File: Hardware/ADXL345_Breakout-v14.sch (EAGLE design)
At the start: 10 parts, among them U2 ADXL345PATRICK

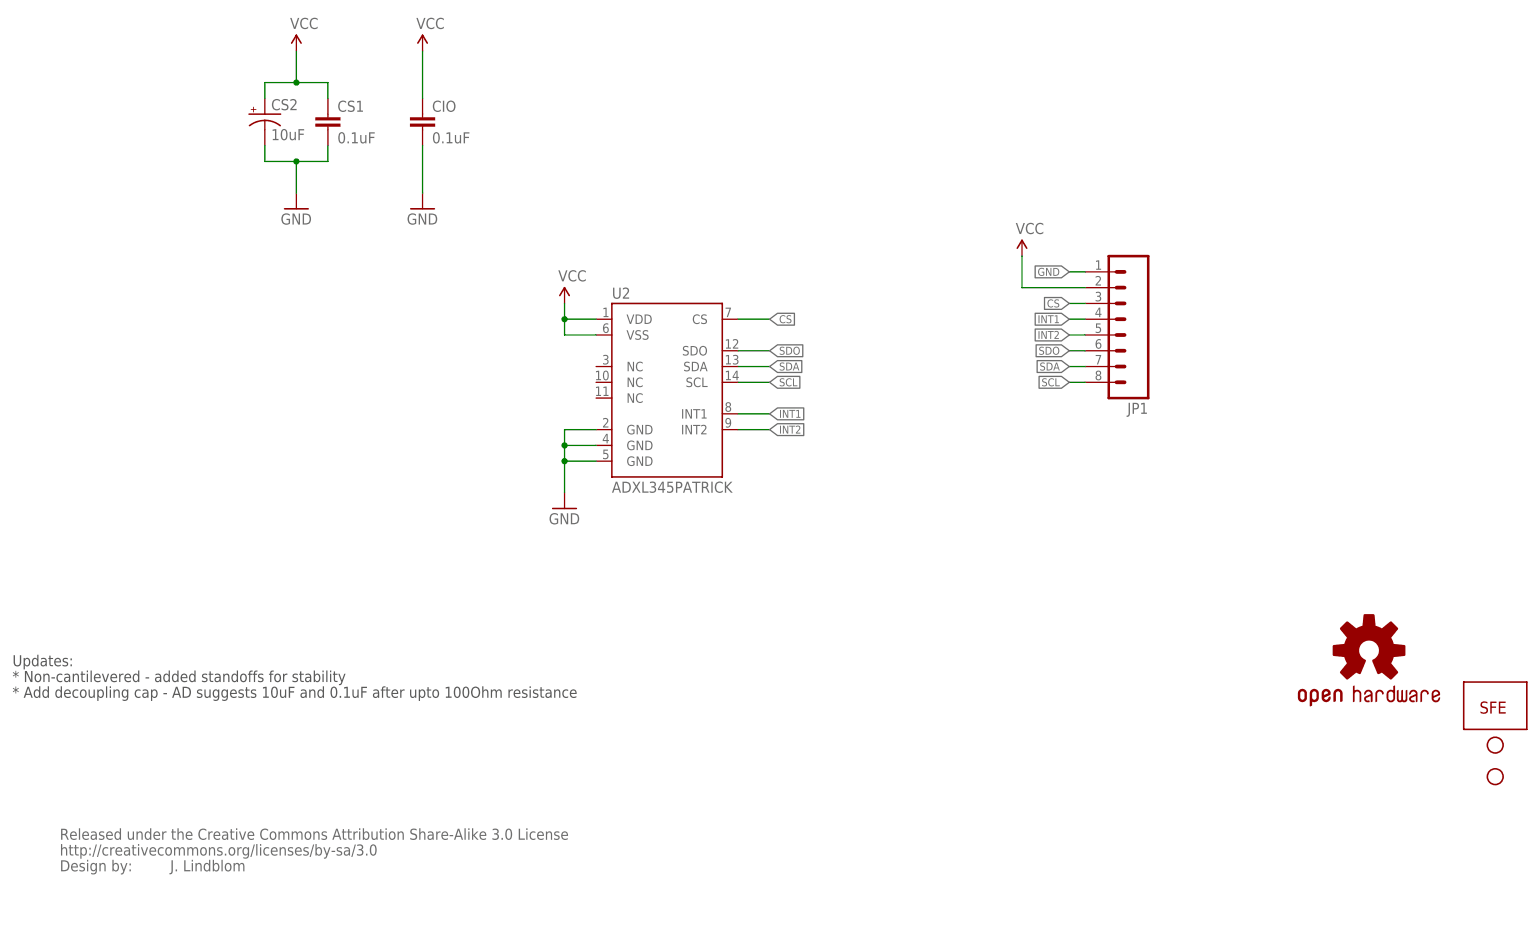
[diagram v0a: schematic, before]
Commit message: Schematic Change, CAP Names, Package Move
Updated to Frame Letter for the Schematic, Changed Caps names to C2, C1
and Moved the ADXL345 package to make more room for the 10uf Cap.
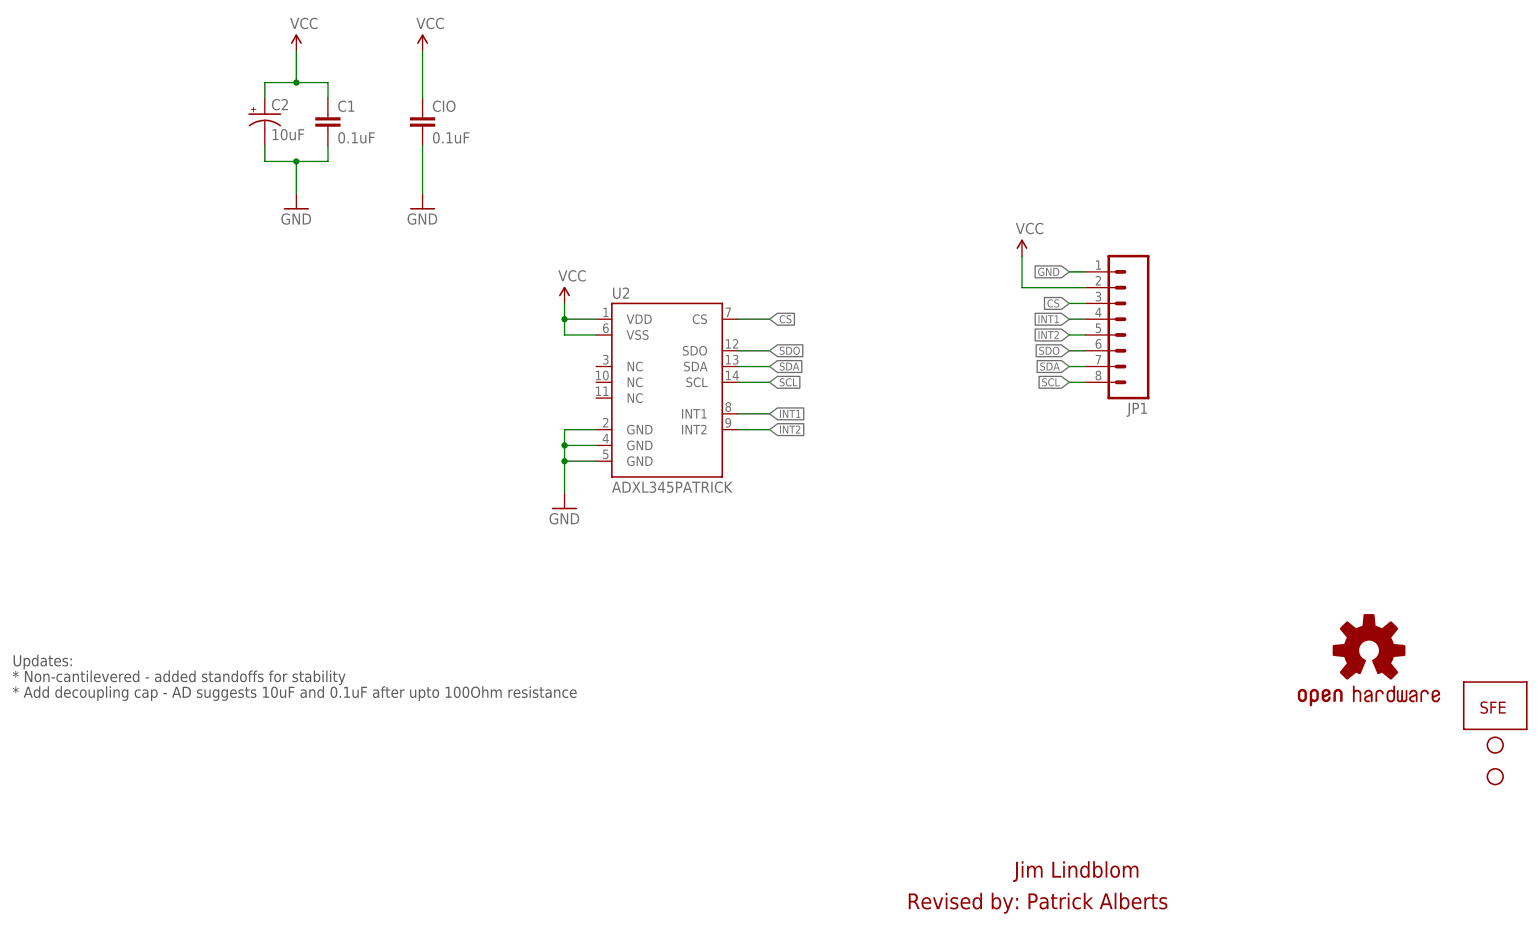
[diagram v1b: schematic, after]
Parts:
- removed U$1: CREATIVE_COMMONS, SparkFun:CREATIVE_COMMONS
- renumbered CS1 to C1, CS2 to C2
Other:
- note added: "Jim Lindblom"
- note added: "Revised by: Patrick Alberts"
- note removed: "J. Lindblom"

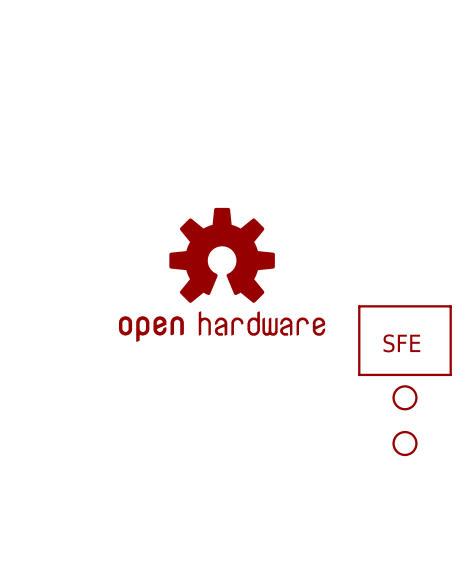
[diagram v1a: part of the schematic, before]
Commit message: Added fiducials
Forgot to put these on the protos, fiducials now added.
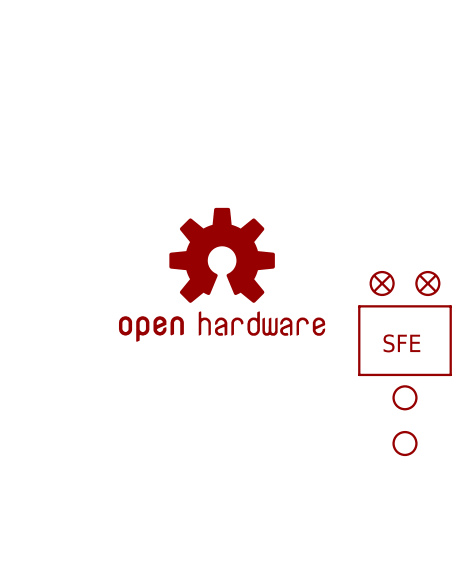
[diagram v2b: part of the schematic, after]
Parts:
- added JP4, JP5: FIDUCIAL1X2, SparkFun-Aesthetics:FIDUCIAL1X2
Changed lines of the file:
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@@
 <grid distance="0.1" unitdist="inch" unit="inch" style="lines" multiple="1" display="no" altdistance="0.01" altunitdist="inch" altunit="inch"/>
 <layers>
-<layer number="1" name="Top" color="4" fill="1" visible="yes" active="no"/>
-<layer number="2" name="Route2" color="1" fill="3" visible="yes" active="no"/>
-<layer number="3" name="Route3" color="4" fill="3" visible="yes" active="no"/>
-<layer number="4" name="Route4" color="1" fill="4" visible="yes" active="no"/>
-<layer number="5" name="Route5" color="4" fill="4" visible="yes" active="no"/>
-<layer number="6" name="Route6" color="1" fill="8" visible="yes" active="no"/>
-<layer number="7" name="Route7" color="4" fill="8" visible="yes" active="no"/>
-<layer number="8" name="Route8" color="1" fill="2" visible="yes" active="no"/>
-<layer number="9" name="Route9" color="4" fill="2" visible="yes" active="no"/>
-<layer number="10" name="Route10" color="1" fill="7" visible="yes" active="no"/>
-<layer number="11" name="Route11" color="4" fill="7" visible="yes" active="no"/>
-<layer number="12" name="Route12" color="1" fill="5" visible="yes" active="no"/>
-<layer number="13" name="Route13" color="4" fill="5" visible="yes" active="no"/>
-<layer number="14" name="Route14" color="1" fill="6" visible="yes" active="no"/>
-<layer number="15" name="Route15" color="4" fill="6" visible="yes" active="no"/>
-<layer number="16" name="Bottom" color="1" fill="1" visible="yes" active="no"/>
-<layer number="17" name="Pads" color="2" fill="1" visible="yes" active="no"/>
-<layer number="18" name="Vias" color="2" fill="1" visible="yes" active="no"/>
-<layer number="19" name="Unrouted" color="6" fill="1" visible="yes" active="no"/>
-<layer number="20" name="Dimension" color="15" fill="1" visible="yes" active="no"/>
-<layer number="21" name="tPlace" color="16" fill="1" visible="yes" active="no"/>
-<layer number="22" name="bPlace" color="14" fill="1" visible="yes" active="no"/>
-<layer number="23" name="tOrigins" color="15" fill="1" visible="yes" active="no"/>
-<layer number="24" name="bOrigins" color="15" fill="1" visible="yes" active="no"/>
-<layer number="25" name="tNames" color="7" fill="1" visible="yes" active="no"/>
-<layer number="26" name="bNames" color="7" fill="1" visible="yes" active="no"/>
-<layer number="27" name="tValues" color="7" fill="1" visible="yes" active="no"/>
-<layer number="28" name="bValues" color="7" fill="1" visible="yes" active="no"/>
+<layer number="1" name="Top" color="4" fill="1" visible="no" active="no"/>
+<layer number="2" name="Route2" color="1" fill="3" visible="no" active="no"/>
+<layer number="3" name="Route3" color="4" fill="3" visible="no" active="no"/>
+<layer number="4" name="Route4" color="1" fill="4" visible="no" active="no"/>
+<layer number="5" name="Route5" color="4" fill="4" visible="no" active="no"/>
+<layer number="6" name="Route6" color="1" fill="8" visible="no" active="no"/>
+<layer number="7" name="Route7" color="4" fill="8" visible="no" active="no"/>
+<layer number="8" name="Route8" color="1" fill="2" visible="no" active="no"/>
+<layer number="9" name="Route9" color="4" fill="2" visible="no" active="no"/>
+<layer number="10" name="Route10" color="1" fill="7" visible="no" active="no"/>
+<layer number="11" name="Route11" color="4" fill="7" visible="no" active="no"/>
+<layer number="12" name="Route12" color="1" fill="5" visible="no" active="no"/>
+<layer number="13" name="Route13" color="4" fill="5" visible="no" active="no"/>
+<layer number="14" name="Route14" color="1" fill="6" visible="no" active="no"/>
+<layer number="15" name="Route15" color="4" fill="6" visible="no" active="no"/>
+<layer number="16" name="Bottom" color="1" fill="1" visible="no" active="no"/>
+<layer number="17" name="Pads" color="2" fill="1" visible="no" active="no"/>
+<layer number="18" name="Vias" color="2" fill="1" visible="no" active="no"/>
+<layer number="19" name="Unrouted" color="6" fill="1" visible="no" active="no"/>
+<layer number="20" name="Dimension" color="15" fill="1" visible="no" active="no"/>
+<layer number="21" name="tPlace" color="16" fill="1" visible="no" active="no"/>
+<layer number="22" name="bPlace" color="14" fill="1" visible="no" active="no"/>
+<layer number="23" name="tOrigins" color="15" fill="1" visible="no" active="no"/>
+<layer number="24" name="bOrigins" color="15" fill="1" visible="no" active="no"/>
+<layer number="25" name="tNames" color="7" fill="1" visible="no" active="no"/>
+<layer number="26" name="bNames" color="7" fill="1" visible="no" active="no"/>
+<layer number="27" name="tValues" color="7" fill="1" visible="no" active="no"/>
+<layer number="28" name="bValues" color="7" fill="1" visible="no" active="no"/>
 <layer number="29" name="tStop" color="7" fill="3" visible="no" active="no"/>
 <layer number="30" name="bStop" color="7" fill="6" visible="no" active="no"/>
@@
 <layer number="35" name="tGlue" color="7" fill="4" visible="no" active="no"/>
 <layer number="36" name="bGlue" color="7" fill="5" visible="no" active="no"/>
-<layer number="37" name="tTest" color="7" fill="1" visible="yes" active="no"/>
-<layer number="38" name="bTest" color="7" fill="1" visible="yes" active="no"/>
+<layer number="37" name="tTest" color="7" fill="1" visible="no" active="no"/>
+<layer number="38" name="bTest" color="7" fill="1" visible="no" active="no"/>
 <layer number="39" name="tKeepout" color="4" fill="11" visible="no" active="no"/>
 <layer number="40" name="bKeepout" color="1" fill="11" visible="no" active="no"/>
@@
 <layer number="44" name="Drills" color="7" fill="1" visible="no" active="no"/>
 <layer number="45" name="Holes" color="7" fill="1" visible="no" active="no"/>
-<layer number="46" name="Milling" color="3" fill="1" visible="yes" active="no"/>
-<layer number="47" name="Measures" color="7" fill="1" visible="yes" active="no"/>
-<layer number="48" name="Document" color="7" fill="1" visible="yes" active="no"/>
-<layer number="49" name="Reference" color="13" fill="1" visible="yes" active="no"/>
-<layer number="50" name="dxf" color="7" fill="1" visible="yes" active="no"/>
-<layer number="51" name="tDocu" color="6" fill="1" visible="yes" active="no"/>
-<layer number="52" name="bDocu" color="7" fill="1" visible="yes" active="no"/>
-<layer number="53" name="tGND_GNDA" color="7" fill="9" visible="yes" active="no"/>
-<layer number="54" name="bGND_GNDA" color="1" fill="9" visible="yes" active="no"/>
-<layer number="56" name="wert" color="7" fill="1" visible="yes" active="no"/>
+<layer number="46" name="Milling" color="3" fill="1" visible="no" active="no"/>
+<layer number="47" name="Measures" color="7" fill="1" visible="no" active="no"/>
+<layer number="48" name="Document" color="7" fill="1" visible="no" active="no"/>
+<layer number="49" name="Reference" color="13" fill="1" visible="no" active="no"/>
+<layer number="50" name="dxf" color="7" fill="1" visible="no" active="no"/>
+<layer number="51" name="tDocu" color="6" fill="1" visible="no" active="no"/>
+<layer number="52" name="bDocu" color="7" fill="1" visible="no" active="no"/>
+<layer number="53" name="tGND_GNDA" color="7" fill="9" visible="no" active="no"/>
+<layer number="54" name="bGND_GNDA" color="1" fill="9" visible="no" active="no"/>
+<layer number="56" name="wert" color="7" fill="1" visible="no" active="no"/>
 <layer number="91" name="Nets" color="2" fill="1" visible="yes" active="yes"/>
 <layer number="92" name="Busses" color="1" fill="1" visible="yes" active="yes"/>
@@
 <part name="U2" library="Testing" deviceset="ADXL345" device="PATRICK"/>
 <part name="FRAME2" library="SparkFun-Aesthetics" deviceset="FRAME-LETTER" device=""/>
+<part name="JP4" library="SparkFun-Aesthetics" deviceset="FIDUCIAL" device="1X2"/>
+<part name="JP5" library="SparkFun-Aesthetics" deviceset="FIDUCIAL" device="1X2"/>
 </parts>
 <sheets>
@@
 <instance part="FRAME2" gate="G$1" x="0" y="0"/>
 <instance part="FRAME2" gate="G$2" x="147.32" y="0"/>
+<instance part="JP4" gate="G$1" x="241.3" y="45.72"/>
+<instance part="JP5" gate="G$1" x="246.38" y="45.72"/>
 </instances>
 <busses>
